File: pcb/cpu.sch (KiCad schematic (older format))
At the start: 9 parts, among them J100 Conn_02x05_Odd_Even, J102 Conn_01x03, U100 LPC5500

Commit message: finish sch rev 0.1
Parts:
- removed J102: Conn_01x03, Connector_PinHeader_2.54mm:PinHeader_1x03_P2.54mm_Vertical, symbol Connector_Generic:Conn_01x03
- removed U100: LPC5500, Package_QFP:TQFP-100-1EP_14x14mm_P0.5mm_EP5x5mm_ThermalVias, symbol symbols:LPC5500
- added U100: LPC5500_FBD64, Package_QFP:LQFP-64-1EP_10x10mm_P0.5mm_EP5x5mm_ThermalVias, symbol symbols:LPC5500_FBD64
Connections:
- net labels added: CHRG, EPD_BUSY, EPD_DC, SPI_MOSI, SPI_SCK, SPI_SSEL0, SW_CE
- net labels removed: ADC1_IN0, BAT_LOW, EXT_PWR_GOOD, FC0_USART_RXD, FC0_USART_TXD, STN_CP, STN_CPG, STN_CPL, STN_D0, STN_D1, STN_FR, STN_S, STN_ST, SW_A, SW_B, SW_SE, SW_ST
- wire segments 69 -> 57
- no-connect marks 2 -> 4
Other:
- note added: "SWO\nSWCLK\nSWDIO"
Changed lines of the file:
@@
 EESchema Schematic File Version 4
-LIBS:pcb-cache
 EELAYER 30 0
 EELAYER END
@@
 Text Notes 8200 5500 0    100  ~ 0
 ARM JTAG
-$Comp
-L power:GND #PWR0124
-U 1 1 5DAAF59A
-P 4900 5000
-F 0 "#PWR0124" H 4900 4750 50  0001 C CNN
-F 1 "GND" H 4905 4827 50  0000 C CNN
-F 2 "" H 4900 5000 50  0001 C CNN
-F 3 "" H 4900 5000 50  0001 C CNN
-	1    4900 5000
-	1    0    0    -1
-$EndComp
-Wire Wire Line
-	5000 4900 4900 4900
-Wire Wire Line
-	4900 4900 4900 5000
 Text GLabel 4200 4400 2    50   Input ~ 0
 PB_STAT
 Wire Wire Line
 	4200 4400 4000 4400
-$Comp
-L Connector_Generic:Conn_01x03 J102
-U 1 1 5D8590D0
-P 5200 4800
-F 0 "J102" H 5280 4842 50  0000 L CNN
-F 1 "Conn_01x03" H 5280 4751 50  0000 L CNN
-F 2 "Connector_PinHeader_2.54mm:PinHeader_1x03_P2.54mm_Vertical" H 5200 4800 50  0001 C CNN
-F 3 "~" H 5200 4800 50  0001 C CNN
-	1    5200 4800
-	1    0    0    -1
-$EndComp
 Text GLabel 6700 2100 2    50   Output ~ 0
 USB_SUSPEND
 Wire Wire Line
 	6700 2100 6500 2100
-Text GLabel 6700 3700 2    50   Output ~ 0
+Text GLabel 4200 3300 2    50   Output ~ 0
 PMIC_ON_REQ
 Wire Wire Line
-	6700 3700 6500 3700
-$Comp
-L symbols:LPC5500 U100
-U 3 1 5D73D2C6
-P 3700 2000
-F 0 "U100" H 3928 696 50  0000 L CNN
-F 1 "LPC5500" H 3928 605 50  0000 L CNN
-F 2 "Package_QFP:TQFP-100-1EP_14x14mm_P0.5mm_EP5x5mm_ThermalVias" H 3700 2400 50  0001 C CNN
-F 3 "" H 3600 2050 50  0001 C CNN
-	3    3700 2000
-	-1   0    0    -1
-$EndComp
-$Comp
-L symbols:LPC5500 U100
-U 4 1 5D73FE0A
-P 6200 2000
-F 0 "U100" H 6428 696 50  0000 L CNN
-F 1 "LPC5500" H 6428 605 50  0000 L CNN
-F 2 "Package_QFP:TQFP-100-1EP_14x14mm_P0.5mm_EP5x5mm_ThermalVias" H 6200 2400 50  0001 C CNN
-F 3 "" H 6100 2050 50  0001 C CNN
-	4    6200 2000
-	-1   0    0    -1
-$EndComp
+	4200 3300 4000 3300
 NoConn ~ 7100 6100
-Wire Wire Line
-	4000 4700 5000 4700
-Wire Wire Line
-	5000 4800 4000 4800
-Text Label 4100 4700 0    50   ~ 0
-FC0_USART_RXD
-Text Label 4100 4800 0    50   ~ 0
-FC0_USART_TXD
-Text GLabel 6700 4900 2    50   Input ~ 0
+Text GLabel 4200 4100 2    50   Input ~ 0
 SAI1_MCLK
 Text GLabel 4200 3900 2    50   Output ~ 0
@@
 Text GLabel 4200 3800 2    50   Output ~ 0
 SAI1_TXD
-Wire Wire Line
-	6500 4900 6700 4900
 Wire Wire Line
 	4000 3800 4200 3800
@@
 Wire Wire Line
 	4000 4100 4200 4100
-Text GLabel 4200 4100 2    50   Input ~ 0
-ADC1_IN0
 Wire Wire Line
 	4200 3400 4000 3400
@@
 ~LCD_PWR_EN
 Wire Wire Line
-	6500 2800 6700 2800
-Wire Wire Line
-	6500 4000 6700 4000
-Wire Wire Line
-	6500 3500 6700 3500
-Wire Wire Line
-	6500 4100 6700 4100
-Wire Wire Line
-	6500 4800 6700 4800
-Wire Wire Line
-	6500 3000 6700 3000
-Wire Wire Line
-	6500 4400 6700 4400
-Text GLabel 6700 4100 2    50   Input ~ 0
+	4000 4600 4200 4600
+Wire Wire Line
+	4000 4700 4200 4700
+Wire Wire Line
+	4000 4500 4200 4500
+Wire Wire Line
+	4000 4800 4200 4800
+Text GLabel 4200 4800 2    50   Input ~ 0
 SW_DN
-Text GLabel 6700 4800 2    50   Input ~ 0
-SW_ST
-Text GLabel 6700 4000 2    50   Input ~ 0
+Text GLabel 4200 4700 2    50   Input ~ 0
 SW_UP
-Text GLabel 6700 2800 2    50   Input ~ 0
+Text GLabel 4200 4600 2    50   Input ~ 0
 SW_LE
-Text GLabel 6700 3000 2    50   Input ~ 0
-SW_A
-Text GLabel 6700 3500 2    50   Input ~ 0
+Text GLabel 4200 4500 2    50   Input ~ 0
 SW_RI
-Text GLabel 6700 4400 2    50   Input ~ 0
-SW_B
-Text GLabel 6700 2900 2    50   Input ~ 0
+Text GLabel 4200 2300 2    50   Input ~ 0
 HOLD
 Wire Wire Line
-	6500 2900 6700 2900
-Wire Wire Line
-	6700 2700 6500 2700
-Wire Wire Line
-	6700 2500 6500 2500
-Wire Wire Line
-	4200 1900 4000 1900
-Wire Wire Line
-	6700 2400 6500 2400
-Wire Wire Line
-	6700 3800 6500 3800
-Wire Wire Line
-	6700 4200 6500 4200
-Wire Wire Line
-	6700 3100 6500 3100
-Wire Wire Line
-	6700 2200 6500 2200
-Text GLabel 6700 2700 2    50   Output ~ 0
-STN_S
-Text GLabel 6700 2500 2    50   Output ~ 0
-STN_FR
-Text GLabel 4200 1900 2    50   Output ~ 0
-STN_CP
-Text GLabel 6700 2400 2    50   Output ~ 0
-STN_D1
-Text GLabel 6700 3800 2    50   Output ~ 0
-STN_D0
-Text GLabel 6700 4200 2    50   Output ~ 0
-STN_ST
-Text GLabel 6700 3100 2    50   Output ~ 0
-STN_CPL
-Text GLabel 6700 2200 2    50   Output ~ 0
-STN_CPG
-Text GLabel 4200 4600 2    50   Input ~ 0
-SW_SE
-Wire Wire Line
-	4000 4600 4200 4600
-Text GLabel 6700 3600 2    50   Input ~ 0
-EXT_PWR_GOOD
-Wire Wire Line
-	6700 3600 6500 3600
+	4000 2300 4200 2300
 Text GLabel 8300 6100 2    50   Output ~ 0
 POR
 Wire Wire Line
 	8100 6100 8300 6100
-Text GLabel 6700 2000 2    50   Input ~ 0
-BAT_LOW
-Wire Wire Line
-	6700 2000 6500 2000
 $Comp
 L Device:LED D?
@@
 Wire Wire Line
 	5800 5950 5800 6050
-Text Label 6700 3400 0    50   ~ 0
+Text Label 4200 1800 0    50   ~ 0
 LED
 Wire Wire Line
-	6500 3400 6850 3400
+	4000 1800 4350 1800
 Text Label 4900 5950 0    50   ~ 0
 LED
@@
 $EndComp
 Connection ~ 4500 1400
-Text GLabel 6700 4600 2    50   Output ~ 0
+Text GLabel 4200 3600 2    50   Output ~ 0
 CODEC_RST
 Wire Wire Line
-	6500 4600 6700 4600
+	4000 3600 4200 3600
+$Comp
+L symbols:LPC5500_FBD64 U100
+U 3 1 5E9E4AC8
+P 3700 2000
+F 0 "U100" H 3642 2465 50  0000 C CNN
+F 1 "LPC5500_FBD64" H 3642 2374 50  0000 C CNN
+F 2 "Package_QFP:LQFP-64-1EP_10x10mm_P0.5mm_EP5x5mm_ThermalVias" H 3700 2400 50  0001 C CNN
+F 3 "" H 3600 2050 50  0001 C CNN
+	3    3700 2000
+	-1   0    0    -1
+$EndComp
+$Comp
+L symbols:LPC5500_FBD64 U100
+U 4 1 5E9EF415
+P 6200 2000
+F 0 "U100" H 6142 2465 50  0000 C CNN
+F 1 "LPC5500_FBD64" H 6142 2374 50  0000 C CNN
+F 2 "Package_QFP:LQFP-64-1EP_10x10mm_P0.5mm_EP5x5mm_ThermalVias" H 6200 2400 50  0001 C CNN
+F 3 "" H 6100 2050 50  0001 C CNN
+	4    6200 2000
+	-1   0    0    -1
+$EndComp
+Text Notes 5450 3000 0    50   ~ 0
+SWO\nSWCLK\nSWDIO
+Text GLabel 4200 2000 2    50   Input ~ 0
+EPD_BUSY
+Text GLabel 4200 2100 2    50   Output ~ 0
+SPI_MOSI
+Text GLabel 4200 2200 2    50   Output ~ 0
+SPI_SSEL0
+Text GLabel 4200 2400 2    50   Output ~ 0
+SPI_SCK
+Wire Wire Line
+	4200 2400 4000 2400
+Wire Wire Line
+	4200 2200 4000 2200
+Wire Wire Line
+	4200 2100 4000 2100
+Wire Wire Line
+	4200 2000 4000 2000
+Text GLabel 6700 2000 2    50   Input ~ 0
+CHRG
+Wire Wire Line
+	6700 2000 6500 2000
+Text GLabel 4200 1900 2    50   Output ~ 0
+EPD_DC
+Wire Wire Line
+	4000 1900 4200 1900
+NoConn ~ 6500 1900
+NoConn ~ 7600 6000
+Text GLabel 4200 4000 2    50   Input ~ 0
+SW_CE
+Wire Wire Line
+	4200 4000 4000 4000
 $EndSCHEMATC

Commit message: rev 0.1
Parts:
- D101: footprint LED_THT:LED_D5.0mm -> LED_SMD:LED_0603_1608Metric
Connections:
- net labels removed: HOLD, SW_CE, ~LCD_PWR_EN
- wire segments 57 -> 53
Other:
- note added: "SWCLK\nSWDIO"
- note removed: "SWO\nSWCLK\nSWDIO"
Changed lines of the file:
@@
 Text Label 4800 2900 0    50   ~ 0
 MPU_JTAG_TCK
-Text Label 4800 2800 0    50   ~ 0
-MPU_JTAG_TDO
 Text Label 4800 3000 0    50   ~ 0
 MPU_JTAG_TMS
@@
 Text Notes 8200 5500 0    100  ~ 0
 ARM JTAG
-Text GLabel 4200 4400 2    50   Input ~ 0
+Text GLabel 6700 2100 2    50   Input ~ 0
 PB_STAT
 Wire Wire Line
+	6700 2100 6500 2100
+Text GLabel 4200 4400 2    50   Output ~ 0
+USB_SUSPEND
+Wire Wire Line
 	4200 4400 4000 4400
-Text GLabel 6700 2100 2    50   Output ~ 0
-USB_SUSPEND
-Wire Wire Line
-	6700 2100 6500 2100
-Text GLabel 4200 3300 2    50   Output ~ 0
+Text GLabel 4200 4500 2    50   Output ~ 0
 PMIC_ON_REQ
 Wire Wire Line
-	4200 3300 4000 3300
+	4200 4500 4000 4500
 NoConn ~ 7100 6100
 Text GLabel 4200 4100 2    50   Input ~ 0
@@
 I2C1_SCL
 Wire Wire Line
-	4000 2800 5400 2800
-Wire Wire Line
 	4000 2900 5400 2900
 Wire Wire Line
@@
 	4000 4100 4200 4100
 Wire Wire Line
-	4200 3400 4000 3400
-Text GLabel 4200 3400 2    50   Output ~ 0
-~LCD_PWR_EN
-Wire Wire Line
-	4000 4600 4200 4600
+	4000 2300 4200 2300
+Wire Wire Line
+	4000 4000 4200 4000
+Wire Wire Line
+	4000 4800 4200 4800
 Wire Wire Line
 	4000 4700 4200 4700
-Wire Wire Line
-	4000 4500 4200 4500
-Wire Wire Line
-	4000 4800 4200 4800
+Text GLabel 4200 4700 2    50   Input ~ 0
+SW_DN
+Text GLabel 4200 4000 2    50   Input ~ 0
+SW_UP
+Text GLabel 4200 2300 2    50   Input ~ 0
+SW_LE
 Text GLabel 4200 4800 2    50   Input ~ 0
-SW_DN
-Text GLabel 4200 4700 2    50   Input ~ 0
-SW_UP
-Text GLabel 4200 4600 2    50   Input ~ 0
-SW_LE
-Text GLabel 4200 4500 2    50   Input ~ 0
 SW_RI
-Text GLabel 4200 2300 2    50   Input ~ 0
-HOLD
-Wire Wire Line
-	4000 2300 4200 2300
 Text GLabel 8300 6100 2    50   Output ~ 0
 POR
@@
 F 0 "D101" H 5200 6050 50  0000 C CNN
 F 1 "LED" H 5350 6050 50  0000 C CNN
-F 2 "LED_THT:LED_D5.0mm" H 5250 5950 50  0001 C CNN
+F 2 "LED_SMD:LED_0603_1608Metric" H 5250 5950 50  0001 C CNN
 F 3 "~" H 5250 5950 50  0001 C CNN
 	1    5250 5950
@@
 Wire Wire Line
 	5800 5950 5800 6050
-Text Label 4200 1800 0    50   ~ 0
+Text Label 4200 2800 0    50   ~ 0
 LED
 Wire Wire Line
-	4000 1800 4350 1800
+	4000 2800 4350 2800
 Text Label 4900 5950 0    50   ~ 0
 LED
@@
 U 3 1 5E9E4AC8
 P 3700 2000
+AR Path="/5E9E4AC8" Ref="U100"  Part="3"
+AR Path="/5D180A01/5E9E4AC8" Ref="U100"  Part="3"
 F 0 "U100" H 3642 2465 50  0000 C CNN
 F 1 "LPC5500_FBD64" H 3642 2374 50  0000 C CNN
@@
 U 4 1 5E9EF415
 P 6200 2000
+AR Path="/5E9EF415" Ref="U100"  Part="4"
+AR Path="/5D180A01/5E9EF415" Ref="U100"  Part="4"
 F 0 "U100" H 6142 2465 50  0000 C CNN
 F 1 "LPC5500_FBD64" H 6142 2374 50  0000 C CNN
@@
 $EndComp
 Text Notes 5450 3000 0    50   ~ 0
-SWO\nSWCLK\nSWDIO
+SWCLK\nSWDIO
 Text GLabel 4200 2000 2    50   Input ~ 0
 EPD_BUSY
@@
 NoConn ~ 6500 1900
 NoConn ~ 7600 6000
-Text GLabel 4200 4000 2    50   Input ~ 0
-SW_CE
-Wire Wire Line
-	4200 4000 4000 4000
 $EndSCHEMATC

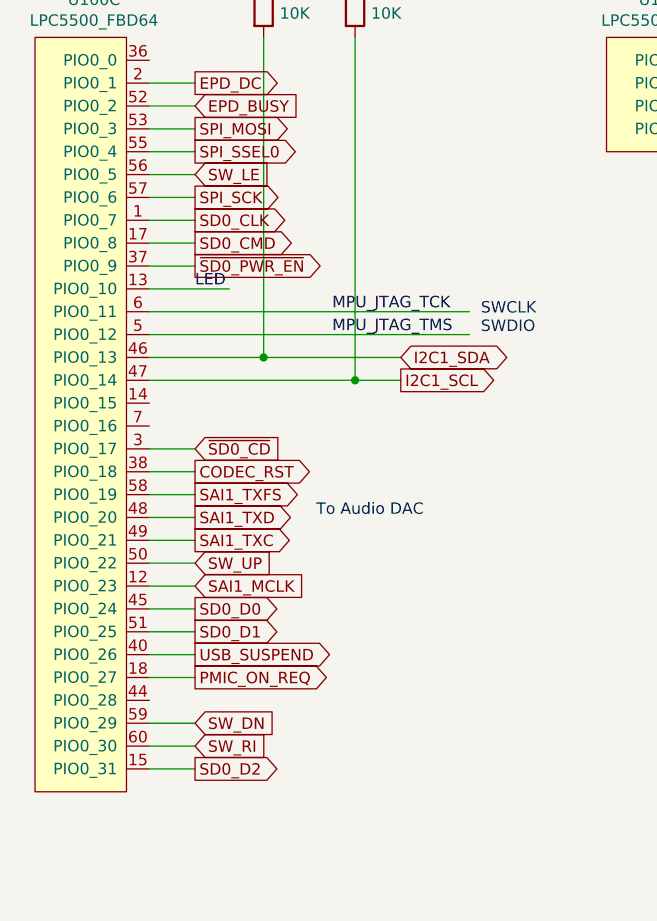
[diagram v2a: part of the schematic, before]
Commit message: pcb: rename keypad signal names
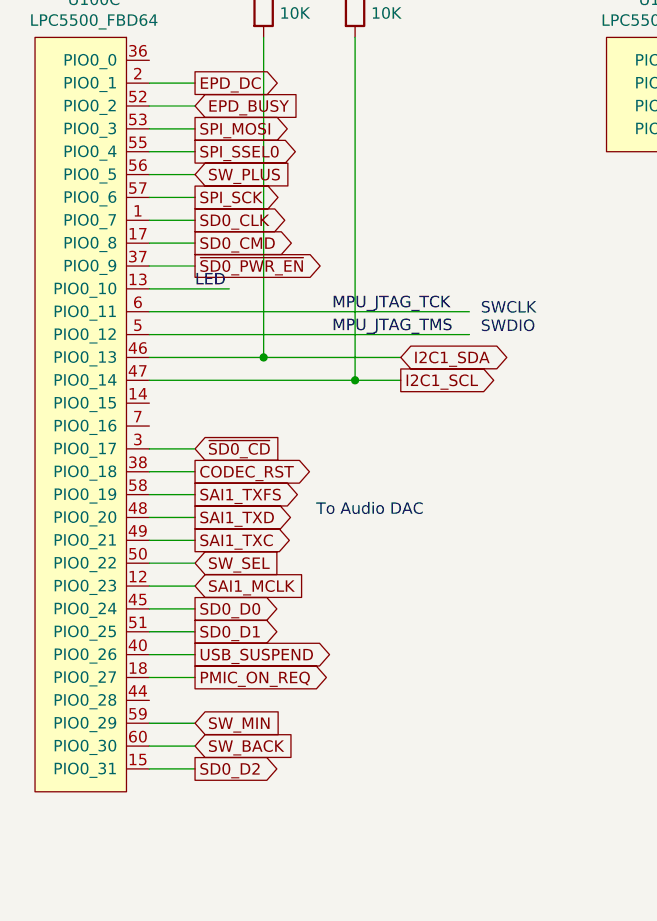
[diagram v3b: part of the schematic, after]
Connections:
- net labels added: SW_BACK, SW_MIN, SW_PLUS, SW_SEL
- net labels removed: SW_DN, SW_LE, SW_RI, SW_UP
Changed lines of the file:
@@
 	4000 4700 4200 4700
 Text GLabel 4200 4700 2    50   Input ~ 0
-SW_DN
+SW_MIN
 Text GLabel 4200 4000 2    50   Input ~ 0
-SW_UP
+SW_SEL
 Text GLabel 4200 2300 2    50   Input ~ 0
-SW_LE
+SW_PLUS
 Text GLabel 4200 4800 2    50   Input ~ 0
-SW_RI
+SW_BACK
 Text GLabel 8300 6100 2    50   Output ~ 0
 POR

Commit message: pcb: bug fixes
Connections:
- net labels added: EPD_RST
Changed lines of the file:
@@
 Text GLabel 4200 4100 2    50   Input ~ 0
 SAI1_MCLK
-Text GLabel 4200 3900 2    50   Output ~ 0
+Text GLabel 4200 3900 2    50   Input ~ 0
 SAI1_TXC
-Text GLabel 4200 3700 2    50   Output ~ 0
+Text GLabel 4200 3700 2    50   Input ~ 0
 SAI1_TXFS
 Text GLabel 4200 3800 2    50   Output ~ 0
@@
 NoConn ~ 6500 1900
 NoConn ~ 7600 6000
+Text GLabel 5100 3500 2    50   Output ~ 0
+EPD_RST
 $EndSCHEMATC

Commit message: pcb: rev 0.2
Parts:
- removed R110, R111: 10K, Resistor_SMD:R_0603_1608Metric, symbol Device:R
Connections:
- net labels added: SD0_PWR_EN
- net labels removed: ~SD0_PWR_EN
- wire segments 53 -> 49
- no-connect marks 4 -> 3
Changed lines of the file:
@@
 To Audio DAC\n
 Text GLabel 4200 2700 2    50   Output ~ 0
-~SD0_PWR_EN
+SD0_PWR_EN
 Text GLabel 4200 2500 2    50   Output ~ 0
 SD0_CLK
@@
 Text GLabel 4200 3500 2    50   Input ~ 0
 ~SD0_CD
-Wire Wire Line
-	4900 1400 4500 1400
-$Comp
-L Device:R R111
-U 1 1 5DA7199D
-P 4900 1550
-F 0 "R111" H 4970 1596 50  0000 L CNN
-F 1 "10K" H 4970 1505 50  0000 L CNN
-F 2 "Resistor_SMD:R_0603_1608Metric" V 4830 1550 50  0001 C CNN
-F 3 "~" H 4900 1550 50  0001 C CNN
-	1    4900 1550
-	1    0    0    -1
-$EndComp
-$Comp
-L Device:R R110
-U 1 1 5DA710EB
-P 4500 1550
-F 0 "R110" H 4570 1596 50  0000 L CNN
-F 1 "10K" H 4570 1505 50  0000 L CNN
-F 2 "Resistor_SMD:R_0603_1608Metric" V 4430 1550 50  0001 C CNN
-F 3 "~" H 4500 1550 50  0001 C CNN
-	1    4500 1550
-	1    0    0    -1
-$EndComp
-Wire Wire Line
-	4000 3100 4500 3100
-Wire Wire Line
-	4500 1700 4500 3100
-Wire Wire Line
-	4900 1700 4900 3200
-Wire Wire Line
-	4000 3200 4900 3200
-Connection ~ 4900 3200
-Wire Wire Line
-	4900 3200 5100 3200
-Connection ~ 4500 3100
-Wire Wire Line
-	4500 3100 5100 3100
 Text GLabel 5100 3100 2    50   BiDi ~ 0
 I2C1_SDA
@@
 Wire Wire Line
 	4900 5950 5100 5950
-$Comp
-L power:+3V3 #PWR0106
-U 1 1 5DB9934B
-P 4500 1400
-F 0 "#PWR0106" H 4500 1250 50  0001 C CNN
-F 1 "+3V3" H 4515 1573 50  0000 C CNN
-F 2 "" H 4500 1400 50  0001 C CNN
-F 3 "" H 4500 1400 50  0001 C CNN
-	1    4500 1400
-	1    0    0    -1
-$EndComp
-Connection ~ 4500 1400
 Text GLabel 4200 3600 2    50   Output ~ 0
 CODEC_RST
@@
 Wire Wire Line
 	4000 1900 4200 1900
-NoConn ~ 6500 1900
 NoConn ~ 7600 6000
-Text GLabel 5100 3500 2    50   Output ~ 0
+Text GLabel 6700 1900 2    50   Output ~ 0
 EPD_RST
+Wire Wire Line
+	4000 3100 5100 3100
+Wire Wire Line
+	4000 3200 5100 3200
+Wire Wire Line
+	6500 1900 6700 1900
 $EndSCHEMATC
